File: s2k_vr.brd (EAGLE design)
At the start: 55.9 x 30.5 mm, 57 parts, among them IC1 MKE04Z8VWJ4, IC2 MAX9926, IC3 LTC6903, IC4 74LVC2G32DP, Q1 12MHz

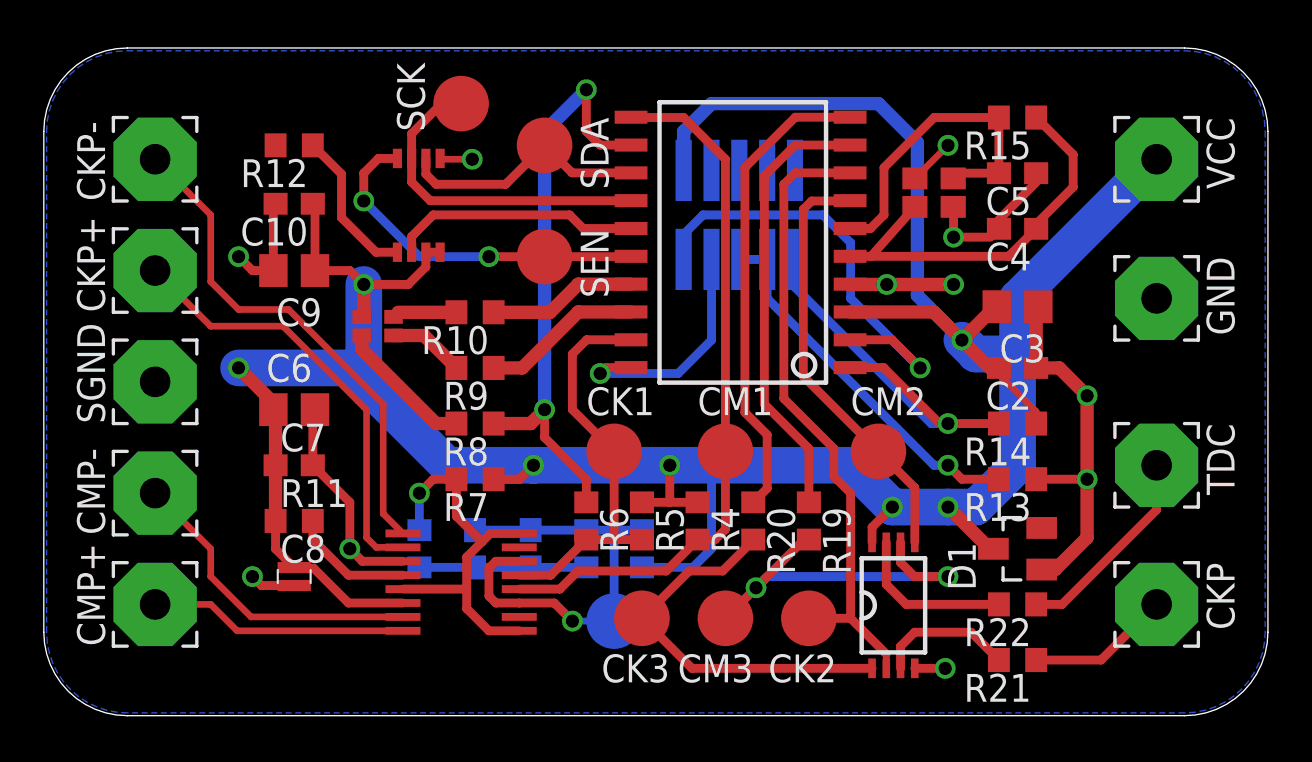
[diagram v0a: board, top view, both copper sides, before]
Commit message: Replace crystal with CX2520DB and reshuffle timer output channels.
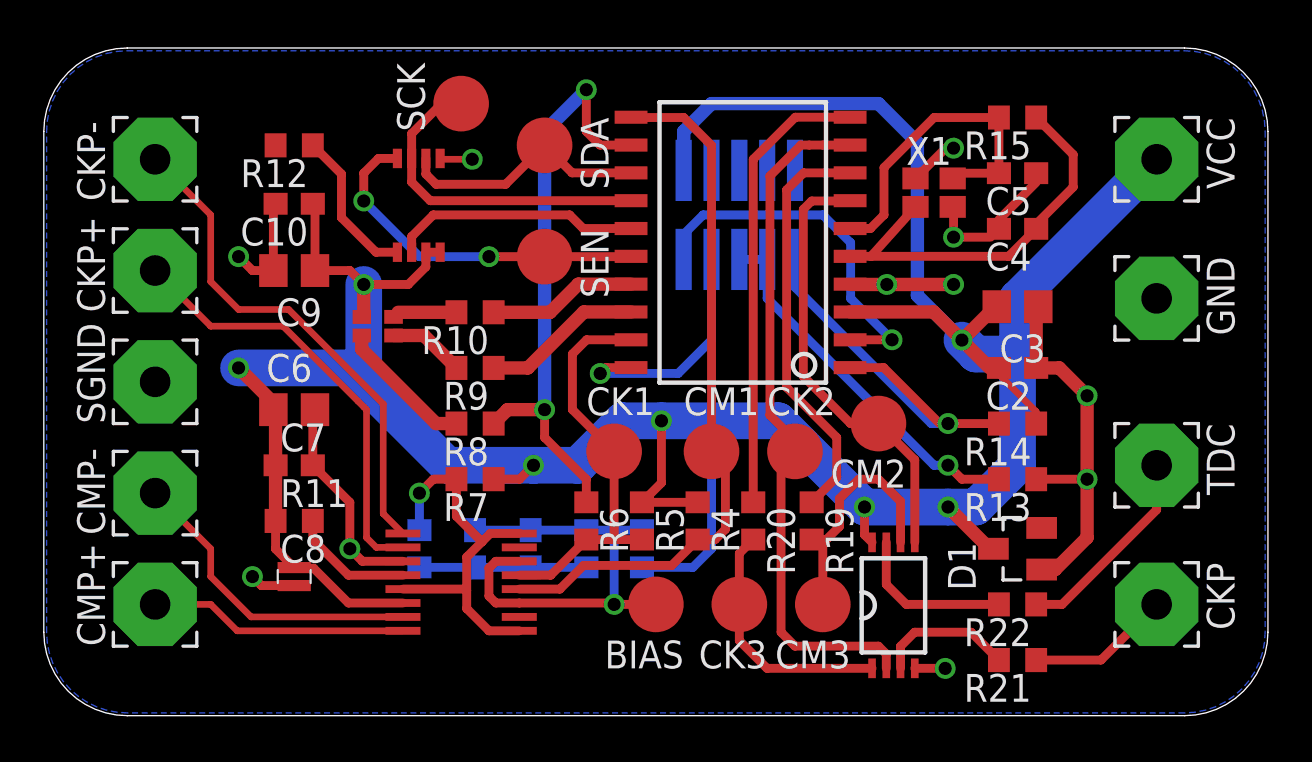
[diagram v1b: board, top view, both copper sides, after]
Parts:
- removed Q1: 12MHz, parts:ABM10-167
- added X1: 12MHz, parts:SMD4-2520
- moved CK2 7.65 mm to (34.3, 12.1), turned to 0 degrees
- moved CM3 4.49 mm to (35.6, 5.08)
- moved CK3 4.49 mm to (31.8, 5.08)
- moved BIAS 2.05 mm to (27.9, 5.08), flipped to the top
- moved CM2 1.27 mm to (38.1, 13.3), turned to 180 degrees
- moved CM1 0.63 mm to (30.5, 12.1)
- moved R19 0.13 mm to (35.1, 8.89)
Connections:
- net CAM_PULSE: now also IC1.9; no longer IC1.8
- net GND: now also X1.2, X1.4; no longer Q1.2, Q1.4
- net N$10: now also X1.1; no longer Q1.1
- net N$15: now also IC1.8; no longer IC1.9
- net N$26: now also X1.3; no longer Q1.3
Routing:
- net N$25: track 17.9 -> 11.2 mm, vias 2 -> 0
- net CAM_TDC: track 18.2 -> 11.5 mm
- net +5V: track 145.7 -> 151.6 mm
- net SWDIO: track 20.4 -> 16.8 mm
- net CAM_PULSE: track 29.2 -> 31.7 mm
- net N$15: track 20.2 -> 18.9 mm
- net N$19: track 20.7 -> 21.6 mm
- net N$17: track 21.7 -> 20.9 mm
